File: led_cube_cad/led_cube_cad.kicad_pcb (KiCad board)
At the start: 2 copper layers, 202.7 x 198.6 mm, 102 parts, among them U1 4099, U2 4099, U3 4099, U4 4099, U5 4099

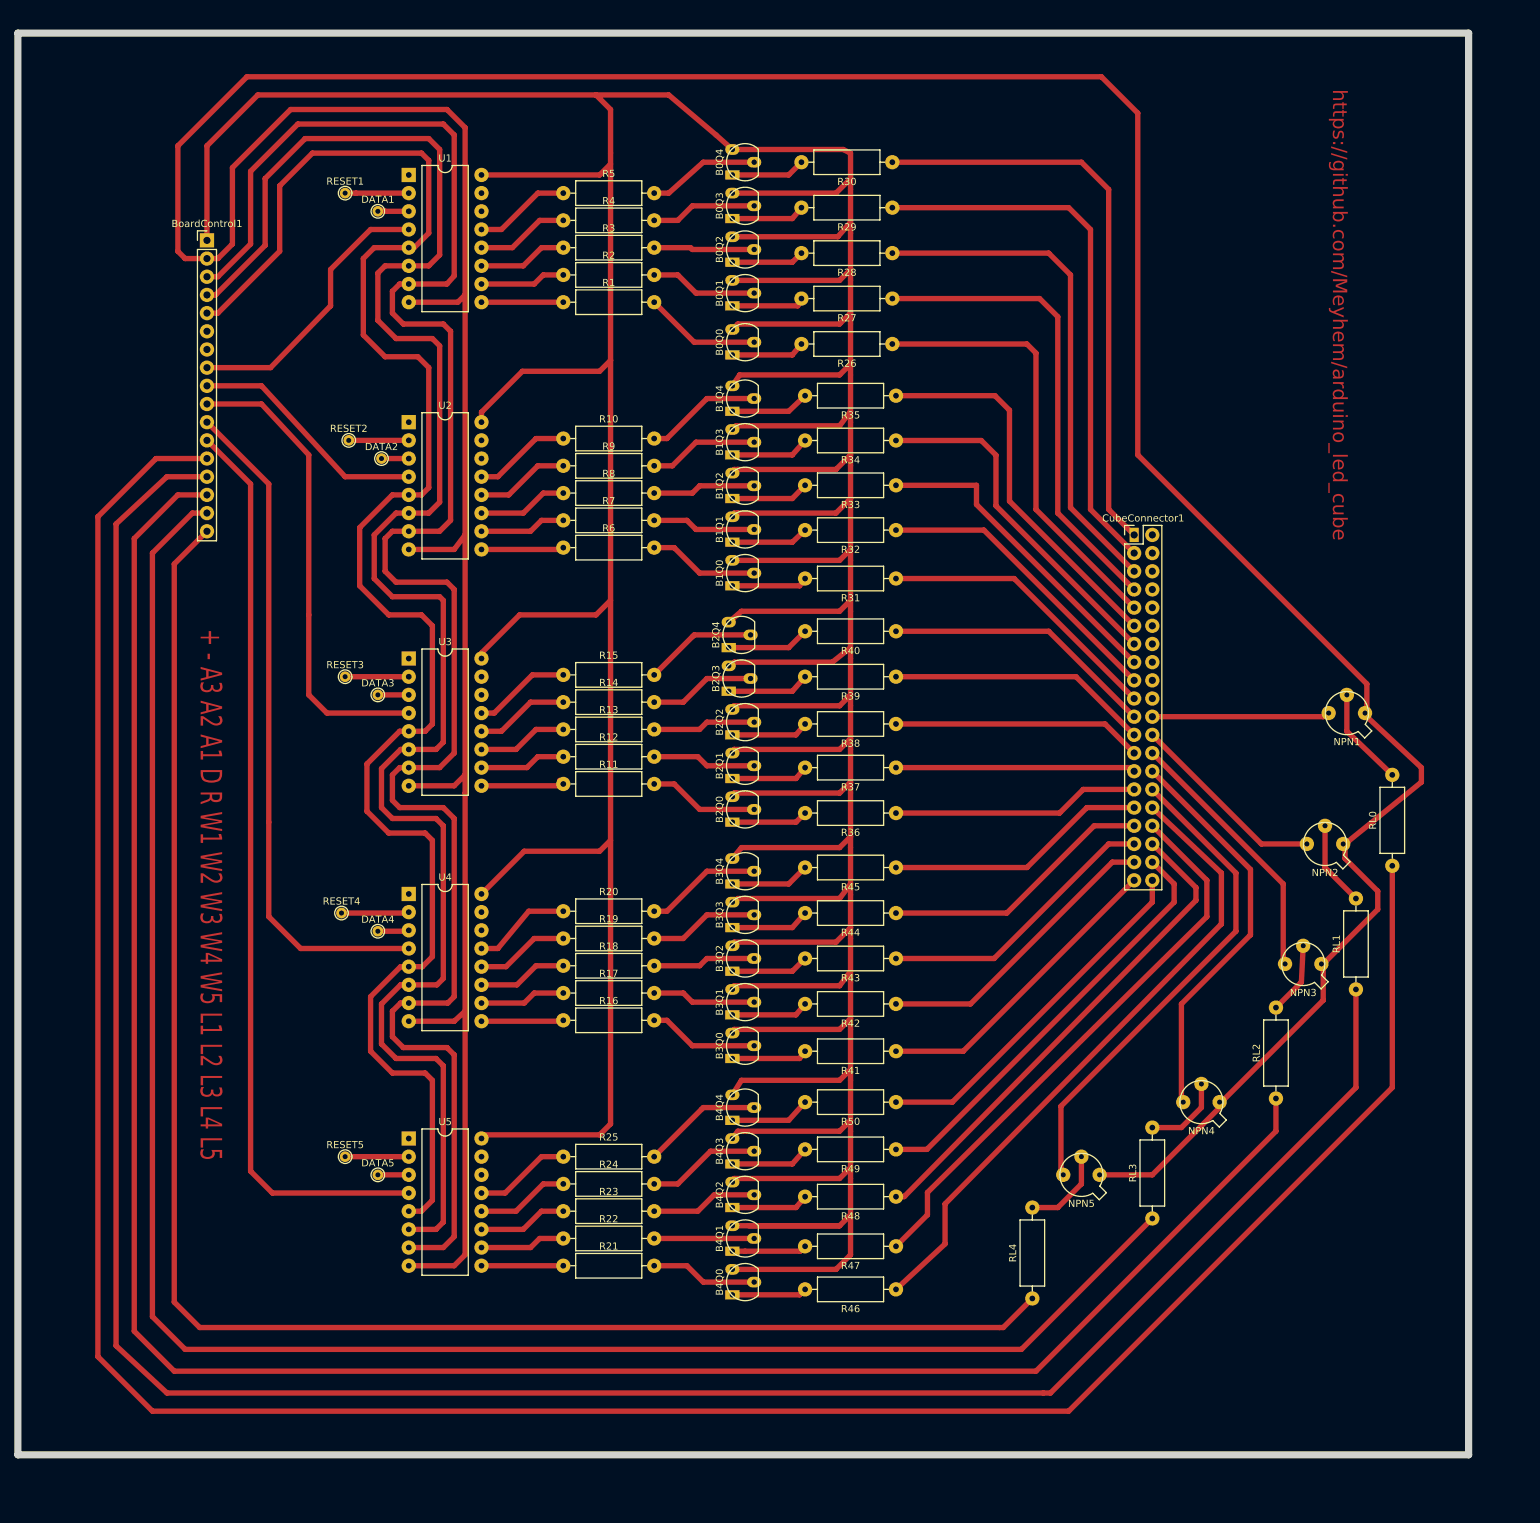
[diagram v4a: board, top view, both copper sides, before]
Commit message: aligned axes, mount holes
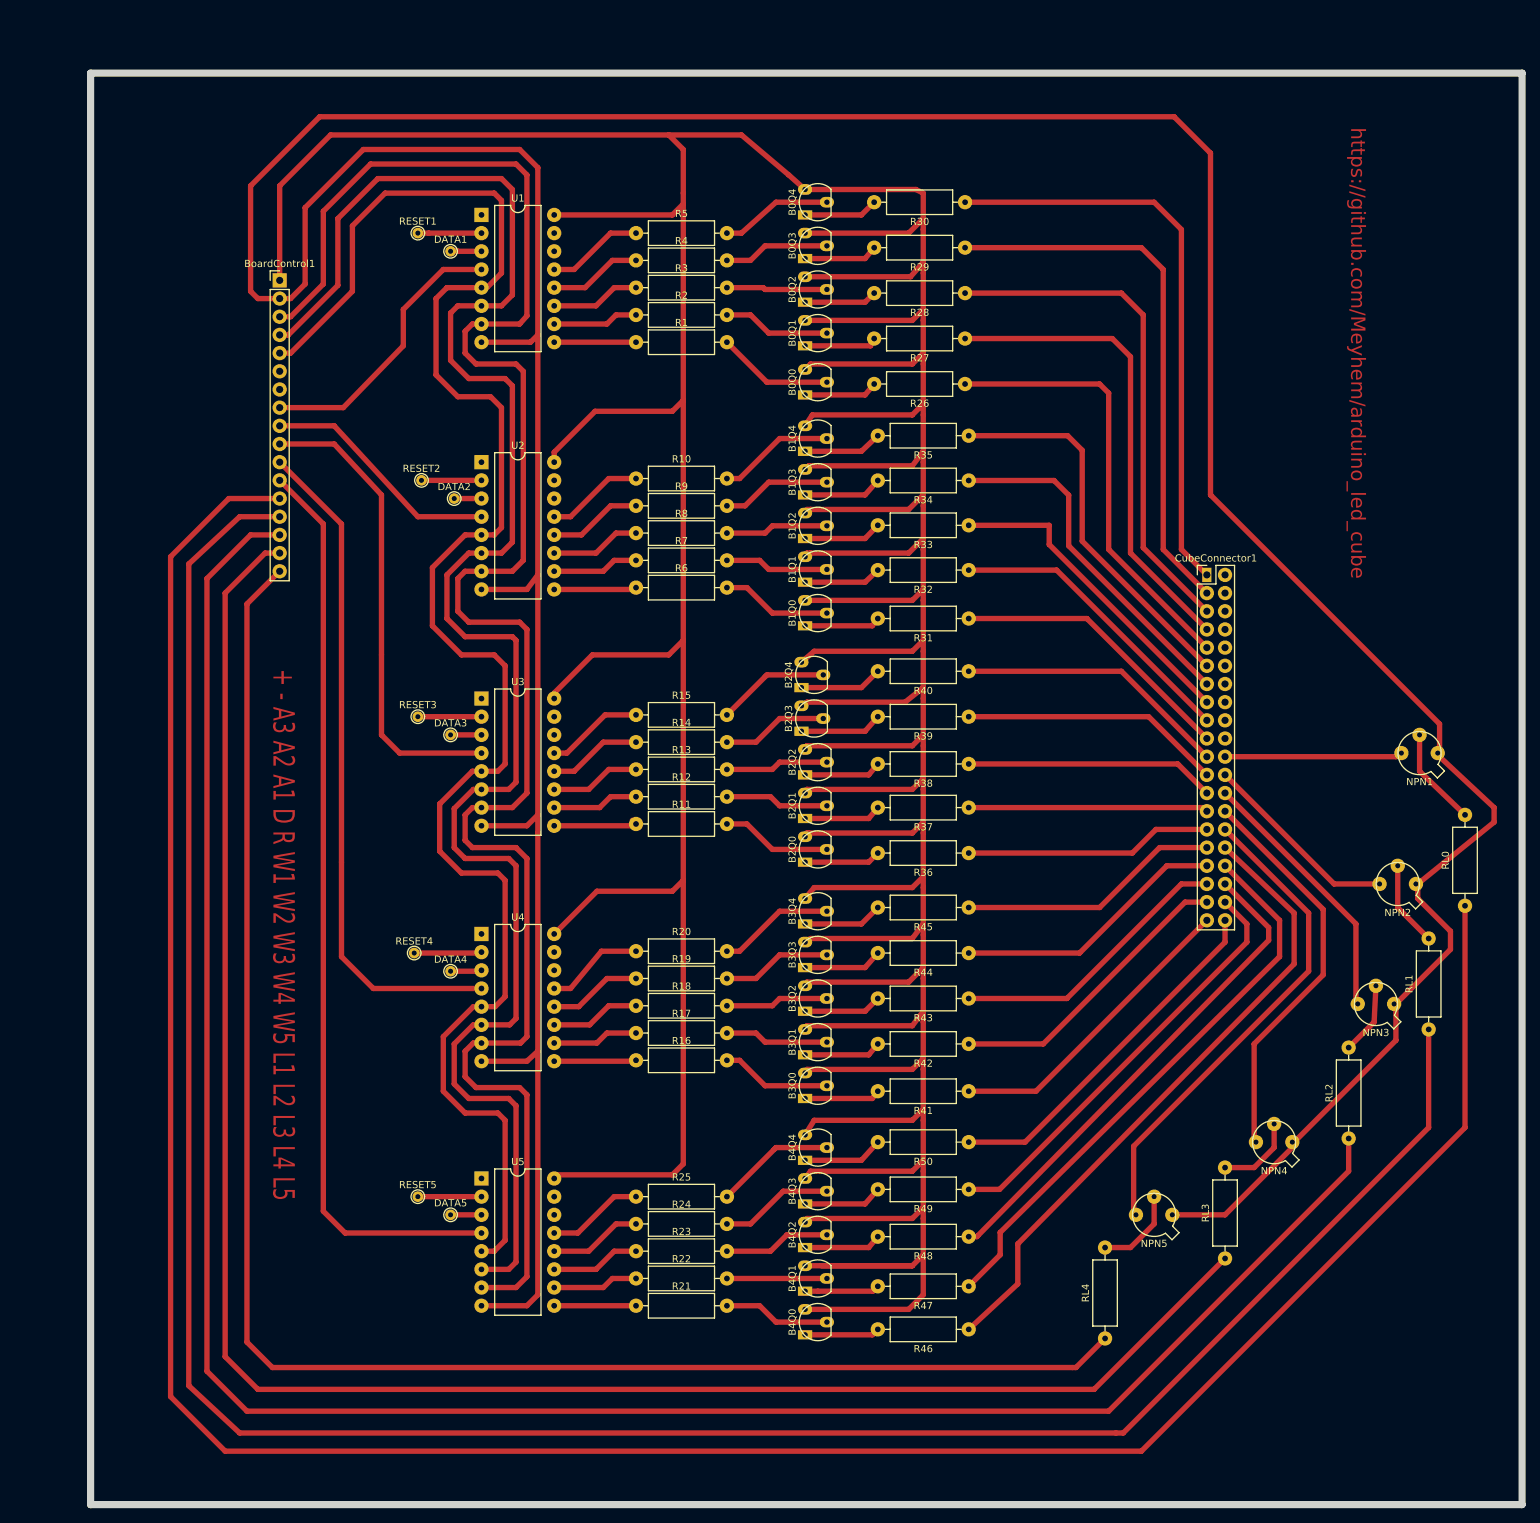
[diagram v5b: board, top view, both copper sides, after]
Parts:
- moved NPN3 11.6 mm to (180.8, 130.0)
- moved NPN5 11.6 mm to (149.9, 159.5)
- moved R27 11.6 mm to (122.2, 37.1)
- moved R26 11.6 mm to (122.2, 43.4)
- moved R28 11.6 mm to (122.2, 30.7)
- moved R29 11.6 mm to (122.2, 24.4)
- moved R30 11.6 mm to (122.2, 18.0)
- moved DATA3 11.6 mm to (50.3, 92.5)
- moved R23 11.6 mm to (76.2, 164.6)
- moved R24 11.6 mm to (76.2, 160.8)
- moved R25 11.6 mm to (76.2, 157.0)
- moved R41 11.6 mm to (122.7, 142.2)
- moved R46 11.6 mm to (122.7, 175.5)
- moved R47 11.6 mm to (122.7, 169.5)
- moved RESET4 11.6 mm to (45.2, 122.9)
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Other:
- board size 202.7 x 198.6 mm -> 200 x 200 mm

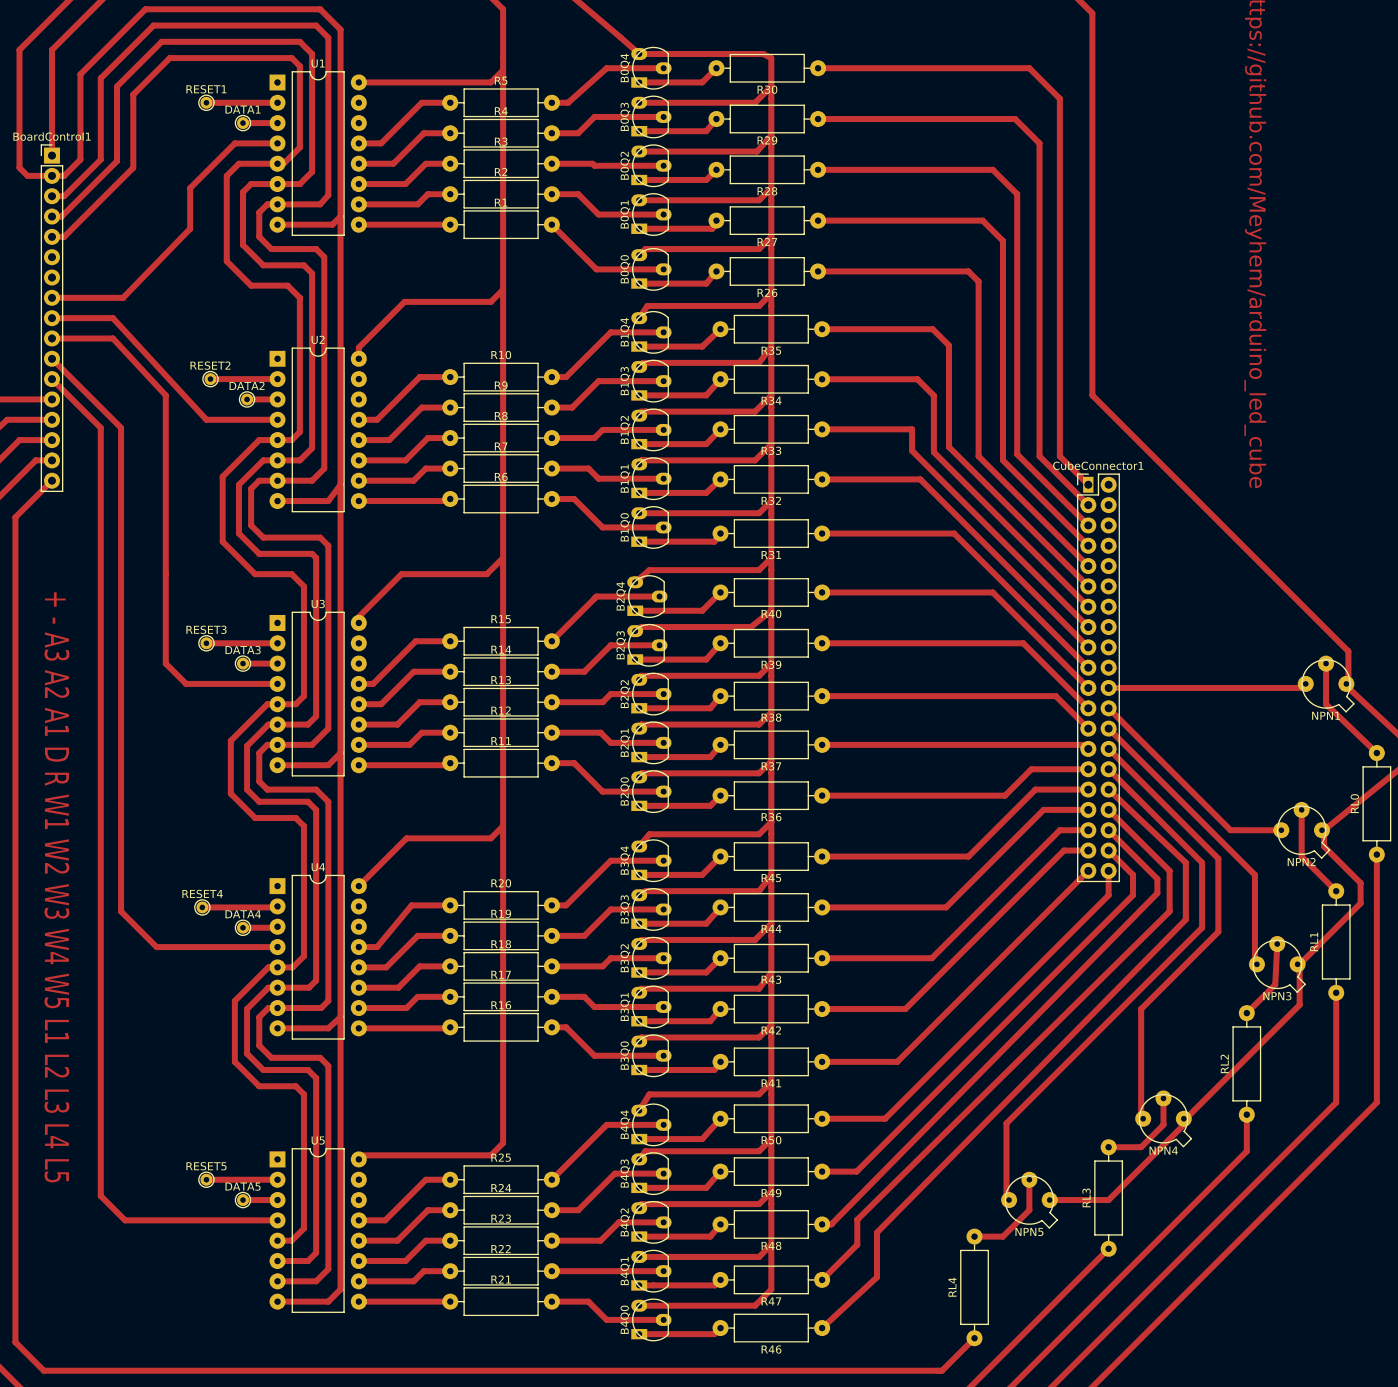
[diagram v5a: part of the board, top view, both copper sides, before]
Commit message: Drill holes
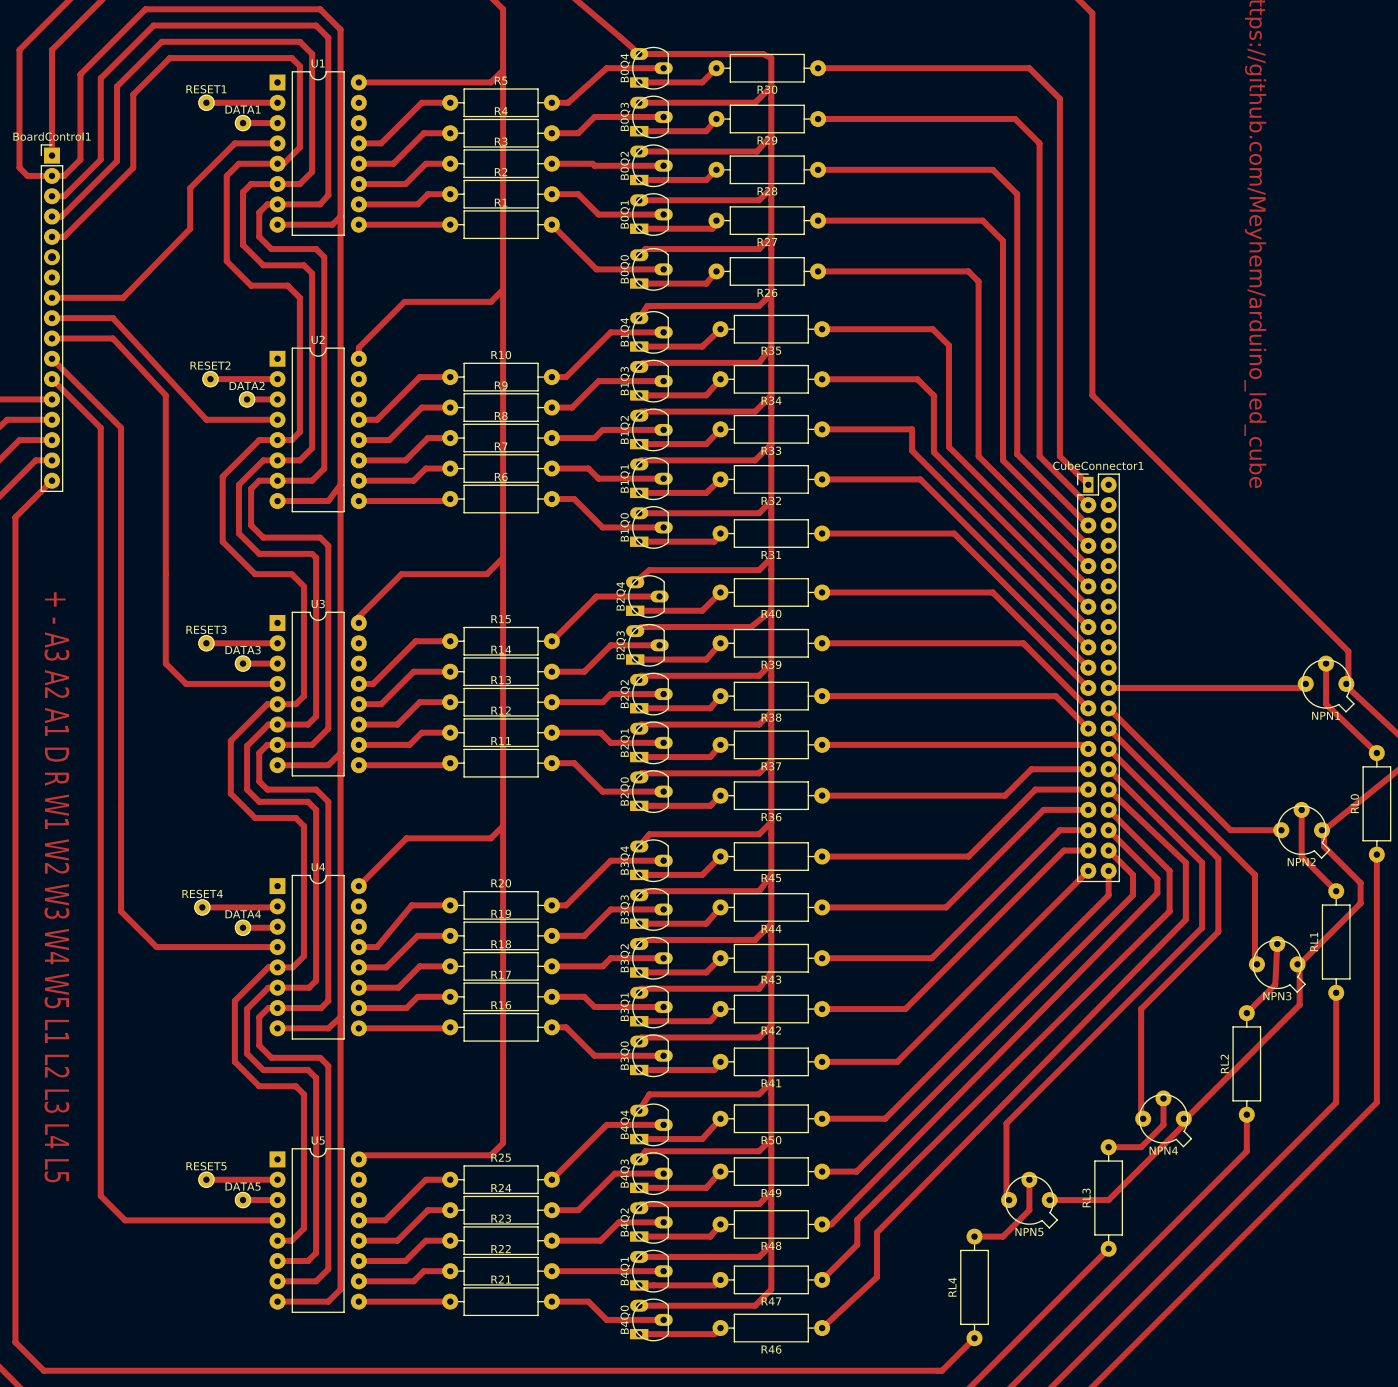
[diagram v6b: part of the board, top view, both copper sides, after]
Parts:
- DATA1, DATA2, DATA3, DATA4, DATA5, RESET1, RESET2, RESET3, RESET4, RESET5: footprint TestPoint:TestPoint_THTPad_D1.5mm_Drill0.7mm -> custom-footprints:TestPoint_THTPad_D2mm_Drill0.8mm

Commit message: funcs
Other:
- board size 200 x 200 mm -> 200 x 196 mm
- board text added: "If you can read this then this is copper side (talking experience)"
